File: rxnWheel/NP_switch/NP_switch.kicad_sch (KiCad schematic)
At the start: 11 parts, among them Q6 IRF7404, Q7 Si4162DY

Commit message: Commit
CoMmMMmMMMmits
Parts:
- added Q?: IRF7404, Package_SO:SOIC-8_3.9x4.9mm_P1.27mm, symbol Transistor_FET:IRF7404
- added Q?: Si4162DY, Package_SO:SOIC-8_3.9x4.9mm_P1.27mm, symbol Transistor_FET:Si4162DY
- added R?: 100, Resistor_SMD:R_0805_2012Metric, symbol Device:R
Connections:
- net OUT_PHASE: now also Q?.5 (D), Q?.5 (D), Q?.6 (D), Q?.6 (D), Q?.7 (D), Q?.7 (D), Q?.8 (D), Q?.8 (D); no longer Q6.1 (S), Q6.2 (S), Q6.3 (S), Q7.5 (D), Q7.6 (D), Q7.7 (D), Q7.8 (D), R30.2
- new net: Q?.1 (S), Q?.2 (S), Q?.3 (S), R?.1
- new net: Q6.1 (S), Q6.2 (S), Q6.3 (S), Q7.5 (D), Q7.6 (D), Q7.7 (D), Q7.8 (D), Q?.1 (S), Q?.2 (S), Q?.3 (S), R30.2
- new net DRV_MTR: Q?.4 (G), Q?.4 (G)
- new net GND: R?.2

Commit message: minor changes
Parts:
- renumbered C15 to C11, C16 to C12, D6 to D2, D7 to D3, Q6 to Q2, Q7 to Q3, R26 to R16, R27 to R17, R28 to R18, R29 to R19, R30 to R20
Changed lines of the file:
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@@
     (effects (font (size 1.27 1.27)) (justify right))
   )
-  (symbol (lib_id "Transistor_FET:IRF7404") (at 151.13 101.6 0)
+  (symbol (lib_id "Transistor_FET:IRF7404") (at 151.13 101.6 0) (unit 1)
     (in_bom yes) (on_board yes) (fields_autoplaced)
     (property "Reference" "Q?" (id 0) (at 157.48 100.3299 0)
@@
     (pin "8")
   )
-  (symbol (lib_id "Device:R") (at 82.55 81.28 0)
-    (in_bom yes) (on_board yes) (fields_autoplaced)
-    (property "Reference" "R29" (id 0) (at 85.09 80.0099 0)
+  (symbol (lib_id "Device:R") (at 82.55 81.28 0) (unit 1)
+    (in_bom yes) (on_board yes) (fields_autoplaced)
+    (property "Reference" "R19" (id 0) (at 85.09 80.0099 0)
       (effects (font (size 1.27 1.27)) (justify left))
     )
@@
     (pin "2")
   )
-  (symbol (lib_id "Device:R") (at 60.96 85.09 90)
-    (in_bom yes) (on_board yes) (fields_autoplaced)
-    (property "Reference" "R27" (id 0) (at 60.96 78.74 90))
+  (symbol (lib_id "Device:R") (at 60.96 85.09 90) (unit 1)
+    (in_bom yes) (on_board yes) (fields_autoplaced)
+    (property "Reference" "R17" (id 0) (at 60.96 78.74 90))
     (property "Value" "100" (id 1) (at 60.96 81.28 90))
     (property "Footprint" "Resistor_SMD:R_0805_2012Metric" (id 2) (at 60.96 86.868 90)
@@
     (pin "2")
   )
-  (symbol (lib_id "Diode:BZV55B12") (at 91.44 106.68 270)
-    (in_bom yes) (on_board yes) (fields_autoplaced)
-    (property "Reference" "D6" (id 0) (at 93.98 105.4099 90)
+  (symbol (lib_id "Diode:BZV55B12") (at 91.44 106.68 270) (unit 1)
+    (in_bom yes) (on_board yes) (fields_autoplaced)
+    (property "Reference" "D2" (id 0) (at 93.98 105.4099 90)
       (effects (font (size 1.27 1.27)) (justify left))
     )
@@
     (pin "2")
   )
-  (symbol (lib_id "power:GND") (at 153.67 116.84 0)
+  (symbol (lib_id "power:GND") (at 153.67 116.84 0) (unit 1)
     (in_bom yes) (on_board yes) (fields_autoplaced)
     (property "Reference" "#PWR?" (id 0) (at 153.67 123.19 0)
@@
     (pin "1")
   )
-  (symbol (lib_id "Device:C") (at 67.31 106.68 0)
-    (in_bom yes) (on_board yes) (fields_autoplaced)
-    (property "Reference" "C15" (id 0) (at 71.12 105.4099 0)
+  (symbol (lib_id "Device:C") (at 67.31 106.68 0) (unit 1)
+    (in_bom yes) (on_board yes) (fields_autoplaced)
+    (property "Reference" "C11" (id 0) (at 71.12 105.4099 0)
       (effects (font (size 1.27 1.27)) (justify left))
     )
@@
     (pin "2")
   )
-  (symbol (lib_id "Device:R") (at 59.69 102.87 90)
-    (in_bom yes) (on_board yes) (fields_autoplaced)
-    (property "Reference" "R26" (id 0) (at 59.69 96.52 90))
+  (symbol (lib_id "Device:R") (at 59.69 102.87 90) (unit 1)
+    (in_bom yes) (on_board yes) (fields_autoplaced)
+    (property "Reference" "R16" (id 0) (at 59.69 96.52 90))
     (property "Value" "100" (id 1) (at 59.69 99.06 90))
     (property "Footprint" "Resistor_SMD:R_0805_2012Metric" (id 2) (at 59.69 104.648 90)
@@
     (pin "2")
   )
-  (symbol (lib_id "Device:R") (at 153.67 111.76 0)
+  (symbol (lib_id "Device:R") (at 153.67 111.76 0) (unit 1)
     (in_bom yes) (on_board yes) (fields_autoplaced)
     (property "Reference" "R?" (id 0) (at 156.21 110.4899 0)
@@
     (pin "2")
   )
-  (symbol (lib_id "Diode:BZV55B12") (at 93.98 81.28 270)
-    (in_bom yes) (on_board yes) (fields_autoplaced)
-    (property "Reference" "D7" (id 0) (at 96.52 80.0099 90)
+  (symbol (lib_id "Diode:BZV55B12") (at 93.98 81.28 270) (unit 1)
+    (in_bom yes) (on_board yes) (fields_autoplaced)
+    (property "Reference" "D3" (id 0) (at 96.52 80.0099 90)
       (effects (font (size 1.27 1.27)) (justify left))
     )
@@
     (pin "2")
   )
-  (symbol (lib_id "Device:C") (at 69.85 81.28 0)
-    (in_bom yes) (on_board yes) (fields_autoplaced)
-    (property "Reference" "C16" (id 0) (at 73.66 80.0099 0)
+  (symbol (lib_id "Device:C") (at 69.85 81.28 0) (unit 1)
+    (in_bom yes) (on_board yes) (fields_autoplaced)
+    (property "Reference" "C12" (id 0) (at 73.66 80.0099 0)
       (effects (font (size 1.27 1.27)) (justify left))
     )
@@
     (pin "2")
   )
-  (symbol (lib_id "Device:R") (at 80.01 106.68 0)
-    (in_bom yes) (on_board yes) (fields_autoplaced)
-    (property "Reference" "R28" (id 0) (at 82.55 105.4099 0)
+  (symbol (lib_id "Device:R") (at 80.01 106.68 0) (unit 1)
+    (in_bom yes) (on_board yes) (fields_autoplaced)
+    (property "Reference" "R18" (id 0) (at 82.55 105.4099 0)
       (effects (font (size 1.27 1.27)) (justify left))
     )
@@
     (pin "2")
   )
-  (symbol (lib_id "Transistor_FET:Si4162DY") (at 107.95 102.87 0)
-    (in_bom yes) (on_board yes) (fields_autoplaced)
-    (property "Reference" "Q7" (id 0) (at 114.3 101.5999 0)
+  (symbol (lib_id "Transistor_FET:Si4162DY") (at 107.95 102.87 0) (unit 1)
+    (in_bom yes) (on_board yes) (fields_autoplaced)
+    (property "Reference" "Q3" (id 0) (at 114.3 101.5999 0)
       (effects (font (size 1.27 1.27)) (justify left))
     )
@@
     (pin "8")
   )
-  (symbol (lib_id "Device:R") (at 124.46 90.17 0)
-    (in_bom yes) (on_board yes) (fields_autoplaced)
-    (property "Reference" "R30" (id 0) (at 127 88.8999 0)
+  (symbol (lib_id "Device:R") (at 124.46 90.17 0) (unit 1)
+    (in_bom yes) (on_board yes) (fields_autoplaced)
+    (property "Reference" "R20" (id 0) (at 127 88.8999 0)
       (effects (font (size 1.27 1.27)) (justify left))
     )
@@
     (pin "2")
   )
-  (symbol (lib_id "Transistor_FET:IRF7404") (at 107.95 85.09 0)
-    (in_bom yes) (on_board yes) (fields_autoplaced)
-    (property "Reference" "Q6" (id 0) (at 114.3 83.8199 0)
+  (symbol (lib_id "Transistor_FET:IRF7404") (at 107.95 85.09 0) (unit 1)
+    (in_bom yes) (on_board yes) (fields_autoplaced)
+    (property "Reference" "Q2" (id 0) (at 114.3 83.8199 0)
       (effects (font (size 1.27 1.27)) (justify left))
     )
@@
     (pin "8")
   )
-  (symbol (lib_id "Transistor_FET:Si4162DY") (at 138.43 91.44 270)
+  (symbol (lib_id "Transistor_FET:Si4162DY") (at 138.43 91.44 270) (unit 1)
     (in_bom yes) (on_board yes) (fields_autoplaced)
     (property "Reference" "Q?" (id 0) (at 138.43 99.06 90))

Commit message: Brake
commmit
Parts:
- removed Q?: Si4162DY, Package_SO:SOIC-8_3.9x4.9mm_P1.27mm, symbol Transistor_FET:Si4162DY
- removed R?: 100, Resistor_SMD:R_0805_2012Metric, symbol Device:R
- added Q?: Si4162DY, Package_SO:SOIC-8_3.9x4.9mm_P1.27mm, symbol Transistor_FET:Si4162DY
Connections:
- net DRV_MTR: now also Q?.4 (G)
- net OUT_PHASE: now also Q?.1 (S), Q?.2 (S), Q?.3 (S), Q?.1 (S), Q?.2 (S), Q?.3 (S); no longer Q?.5 (D), Q?.6 (D), Q?.7 (D), Q?.8 (D)
- net at Q2.1 (S), Q2.2 (S), Q2.3 (S)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: now also Q?.5 (D), Q?.6 (D), Q?.7 (D), Q?.8 (D)
- new net BRK_OUT: Q?.5 (D), Q?.6 (D), Q?.7 (D), Q?.8 (D)
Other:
- moved on the sheet: Q?

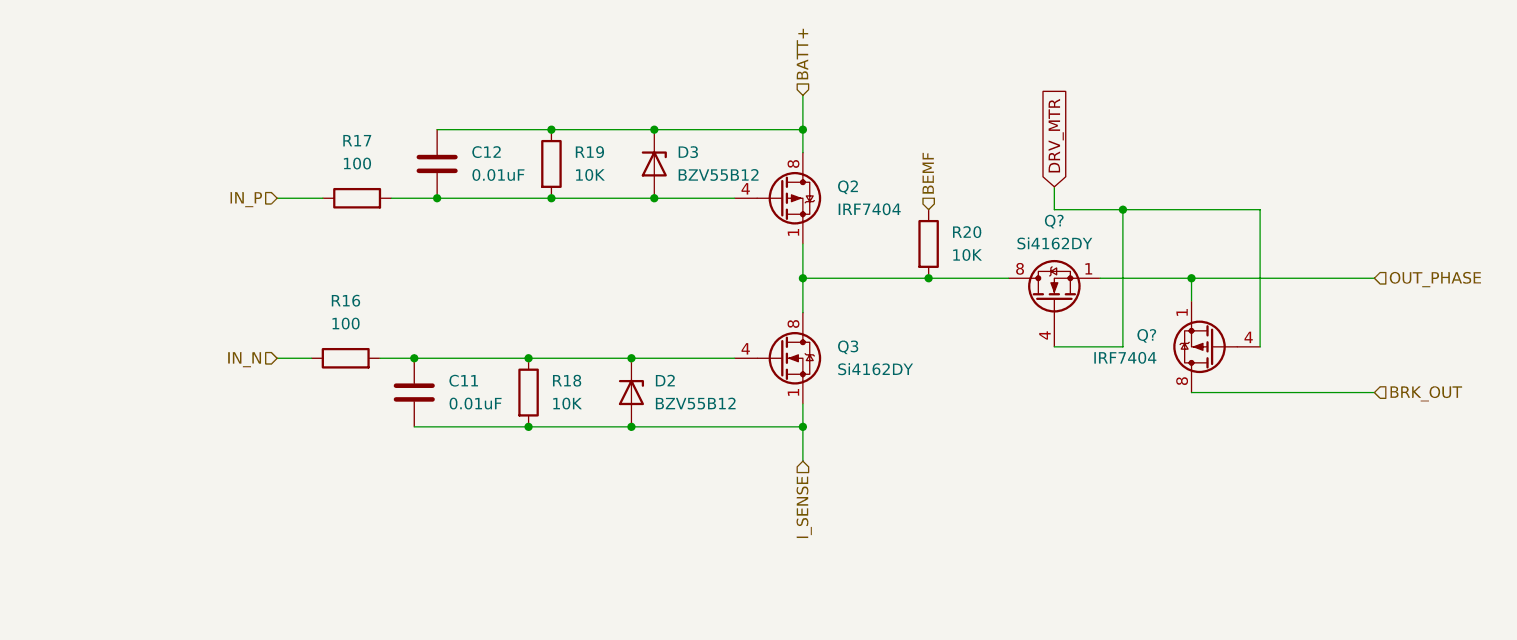
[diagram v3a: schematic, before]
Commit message: LED
led
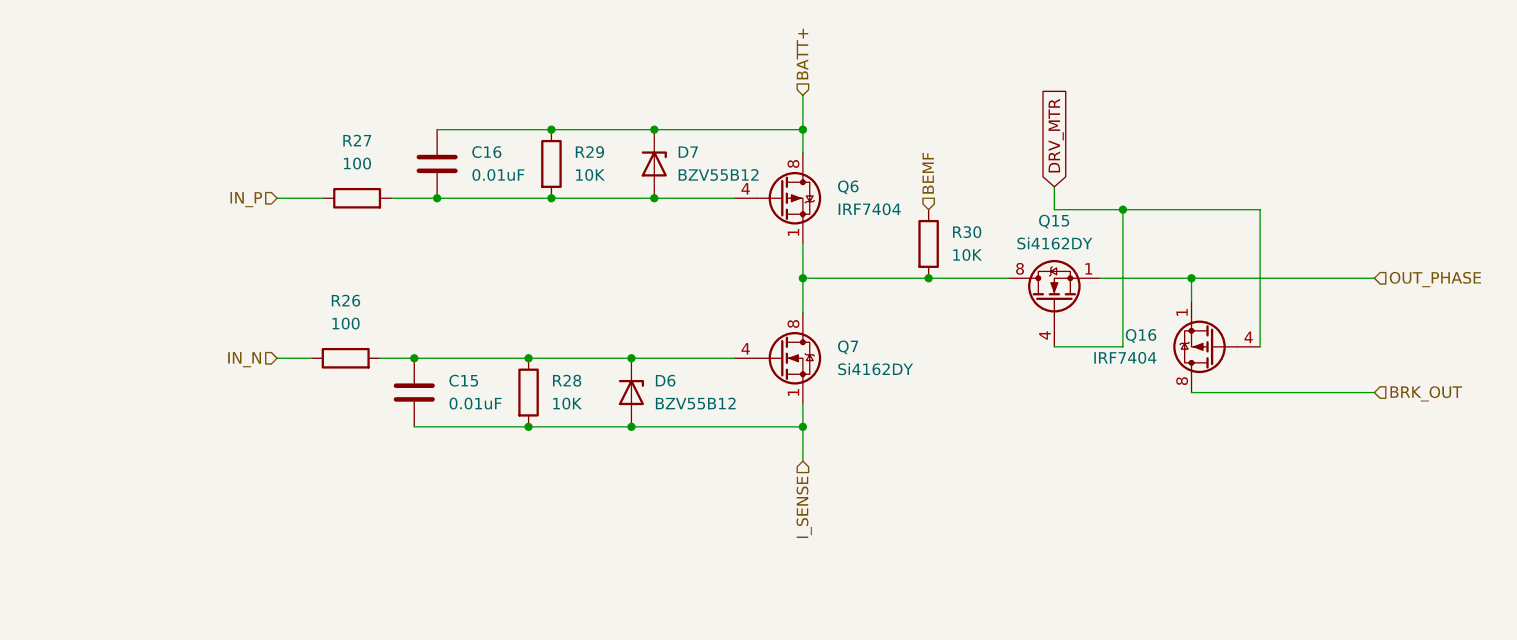
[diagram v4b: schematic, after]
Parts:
- gave numbers to parts that had none: 2
- renumbered C11 to C15, C12 to C16, D2 to D6, D3 to D7, Q2 to Q6, Q3 to Q7, R16 to R26, R17 to R27, R18 to R28, R19 to R29, R20 to R30
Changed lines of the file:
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@@
   (symbol (lib_id "Transistor_FET:IRF7404") (at 156.21 101.6 180)
     (in_bom yes) (on_board yes) (fields_autoplaced)
-    (property "Reference" "Q?" (id 0) (at 149.86 100.3299 0)
+    (property "Reference" "Q16" (id 0) (at 149.86 100.3299 0)
       (effects (font (size 1.27 1.27)) (justify left))
     )
@@
   (symbol (lib_id "Device:R") (at 82.55 81.28 0)
     (in_bom yes) (on_board yes) (fields_autoplaced)
-    (property "Reference" "R19" (id 0) (at 85.09 80.0099 0)
+    (property "Reference" "R29" (id 0) (at 85.09 80.0099 0)
       (effects (font (size 1.27 1.27)) (justify left))
     )
@@
   (symbol (lib_id "Device:R") (at 60.96 85.09 90)
     (in_bom yes) (on_board yes) (fields_autoplaced)
-    (property "Reference" "R17" (id 0) (at 60.96 78.74 90))
+    (property "Reference" "R27" (id 0) (at 60.96 78.74 90))
     (property "Value" "100" (id 1) (at 60.96 81.28 90))
     (property "Footprint" "Resistor_SMD:R_0805_2012Metric" (id 2) (at 60.96 86.868 90)
@@
   (symbol (lib_id "Diode:BZV55B12") (at 91.44 106.68 270)
     (in_bom yes) (on_board yes) (fields_autoplaced)
-    (property "Reference" "D2" (id 0) (at 93.98 105.4099 90)
+    (property "Reference" "D6" (id 0) (at 93.98 105.4099 90)
       (effects (font (size 1.27 1.27)) (justify left))
     )
@@
   (symbol (lib_id "Transistor_FET:Si4162DY") (at 138.43 96.52 90)
     (in_bom yes) (on_board yes)
-    (property "Reference" "Q?" (id 0) (at 138.43 87.63 90))
+    (property "Reference" "Q15" (id 0) (at 138.43 87.63 90))
     (property "Value" "Si4162DY" (id 1) (at 138.43 90.17 90))
     (property "Footprint" "Package_SO:SOIC-8_3.9x4.9mm_P1.27mm" (id 2) (at 140.97 91.44 0)
@@
   (symbol (lib_id "Device:C") (at 67.31 106.68 0)
     (in_bom yes) (on_board yes) (fields_autoplaced)
-    (property "Reference" "C11" (id 0) (at 71.12 105.4099 0)
+    (property "Reference" "C15" (id 0) (at 71.12 105.4099 0)
       (effects (font (size 1.27 1.27)) (justify left))
     )
@@
   (symbol (lib_id "Device:R") (at 59.69 102.87 90)
     (in_bom yes) (on_board yes) (fields_autoplaced)
-    (property "Reference" "R16" (id 0) (at 59.69 96.52 90))
+    (property "Reference" "R26" (id 0) (at 59.69 96.52 90))
     (property "Value" "100" (id 1) (at 59.69 99.06 90))
     (property "Footprint" "Resistor_SMD:R_0805_2012Metric" (id 2) (at 59.69 104.648 90)
@@
   (symbol (lib_id "Diode:BZV55B12") (at 93.98 81.28 270)
     (in_bom yes) (on_board yes) (fields_autoplaced)
-    (property "Reference" "D3" (id 0) (at 96.52 80.0099 90)
+    (property "Reference" "D7" (id 0) (at 96.52 80.0099 90)
       (effects (font (size 1.27 1.27)) (justify left))
     )
@@
   (symbol (lib_id "Device:C") (at 69.85 81.28 0)
     (in_bom yes) (on_board yes) (fields_autoplaced)
-    (property "Reference" "C12" (id 0) (at 73.66 80.0099 0)
+    (property "Reference" "C16" (id 0) (at 73.66 80.0099 0)
       (effects (font (size 1.27 1.27)) (justify left))
     )
@@
   (symbol (lib_id "Device:R") (at 80.01 106.68 0)
     (in_bom yes) (on_board yes) (fields_autoplaced)
-    (property "Reference" "R18" (id 0) (at 82.55 105.4099 0)
+    (property "Reference" "R28" (id 0) (at 82.55 105.4099 0)
       (effects (font (size 1.27 1.27)) (justify left))
     )
@@
   (symbol (lib_id "Transistor_FET:Si4162DY") (at 107.95 102.87 0)
     (in_bom yes) (on_board yes) (fields_autoplaced)
-    (property "Reference" "Q3" (id 0) (at 114.3 101.5999 0)
+    (property "Reference" "Q7" (id 0) (at 114.3 101.5999 0)
       (effects (font (size 1.27 1.27)) (justify left))
     )
@@
   (symbol (lib_id "Device:R") (at 124.46 90.17 0)
     (in_bom yes) (on_board yes) (fields_autoplaced)
-    (property "Reference" "R20" (id 0) (at 127 88.8999 0)
+    (property "Reference" "R30" (id 0) (at 127 88.8999 0)
       (effects (font (size 1.27 1.27)) (justify left))
     )
@@
   (symbol (lib_id "Transistor_FET:IRF7404") (at 107.95 85.09 0)
     (in_bom yes) (on_board yes) (fields_autoplaced)
-    (property "Reference" "Q2" (id 0) (at 114.3 83.8199 0)
-      (effects (font (size 1.27 1.27)) (justify left))
-    )
+    (property "Reference" "Q6" (id 0) (at 114.3 83.8199 0)
+      (effects (font (size 1.27 1.27)) (justify left))
+    )

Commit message: cleanup and corrections
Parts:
- removed R26, R27: 100, Resistor_SMD:R_0805_2012Metric, symbol Device:R
- added Q17: ~, symbol Transistor_BJT:2N3904
- added Q18: 2N3904, Package_TO_SOT_THT:TO-92_Inline, symbol Transistor_BJT:2N3904
- added R1, R2: 100, Resistor_SMD:R_0805_2012Metric, symbol Device:R
- added R11, R12, R4, R5: 10K, Resistor_SMD:R_0805_2012Metric, symbol Device:R
- Q2: renamed from Q6; value IRF7404 -> (none); footprint Package_SO:SOIC-8_3.9x4.9mm_P1.27mm -> (none)
- renumbered C15 to C11, C16 to C12, D6 to D2, D7 to D3, Q15 to Q11, Q16 to Q12, Q7 to Q3, R28 to R18, R29 to R19, R30 to R20
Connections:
- net BATT+: now also Q2.1 (S), Q2.2 (S), Q2.3 (S); no longer Q2.5 (D), Q2.6 (D), Q2.7 (D), Q2.8 (D)
- net IN_N: now also R2.1
- net IN_P: now also R1.1
- net at C12.2, D3.2 (A), Q2.4 (G)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: now also Q17.1 (E), R11.1
- net at C11.1, D2.1 (K), Q3.4 (G)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: now also Q18.1 (E), R12.1
- net at Q11.5 (D), Q11.6 (D), Q11.7 (D)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: now also Q2.5 (D), Q2.6 (D), Q2.7 (D), Q2.8 (D); no longer Q2.1 (S), Q2.2 (S), Q2.3 (S)
- net I_SENSE renamed GND
- net GND: now also R11.2, R12.2, R4.2, R5.2
- new net: Q17.2 (B), R1.2, R4.1
- new net: Q18.2 (B), R2.2, R5.1
- new net +5V: Q17.3 (C), Q18.3 (C)

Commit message: changes
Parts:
- removed C11, C12: 0.01uF, Capacitor_SMD:C_0805_2012Metric, symbol Device:C
- removed D2, D3: BZV55B12, Diode_SMD:D_MiniMELF, symbol Diode:BZV55B12
- removed Q11: Si4162DY, Package_SO:SOIC-8_3.9x4.9mm_P1.27mm, symbol Transistor_FET:Si4162DY
- removed Q17: ~, symbol Transistor_BJT:2N3904
- removed Q18: 2N3904, Package_TO_SOT_THT:TO-92_Inline, symbol Transistor_BJT:2N3904
- removed Q2: (no value), symbol Transistor_FET:IRF7404
- removed R1, R2: 100, Resistor_SMD:R_0805_2012Metric, symbol Device:R
- removed R11, R12, R18, R19, R20, R4, R5: 10K, Resistor_SMD:R_0805_2012Metric, symbol Device:R
- added C? (x4): (no value), Capacitor_SMD:C_0805_2012Metric, symbol Device:C
- added Q? (x2): (no value), symbol Transistor_FET:IRF7404
- added U? (x2): (no value), symbol Driver_FET:MCP14A0902xMNY
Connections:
- net BATT+: now also Q?.1 (S), Q?.2 (S), Q?.3 (S)
- net DRV_MTR: now also Q?.4 (G)
- net GND: now also C?.2, C?.2, C?.2, C?.2, U?.4 (GND), U?.4 (GND), U?.5 (GND), U?.5 (GND), U?.9 (GND), U?.9 (GND)
- net OUT_PHASE: now also Q?.5 (D), Q?.6 (D), Q?.7 (D), Q?.8 (D)
- net at Q3.4 (G): now also U?.6 (OUT), U?.7 (OUT)
- net at Q3.5 (D), Q3.6 (D), Q3.7 (D)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: now also Q?.1 (S), Q?.2 (S), Q?.3 (S), Q?.5 (D), Q?.6 (D), Q?.7 (D), Q?.8 (D)
- new net: Q?.4 (G), U?.6 (OUT), U?.7 (OUT)
- new net IN_H: U?.2 (IN)
- new net IN_L: U?.2 (IN)
- new net VBUS: C?.1, C?.1, C?.1, C?.1, U?.1 (VDD), U?.1 (VDD), U?.3 (EN), U?.3 (EN), U?.8 (VDD), U?.8 (VDD)

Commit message: minor changes
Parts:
- removed Q12: IRF7404, Package_SO:SOIC-8_3.9x4.9mm_P1.27mm, symbol Transistor_FET:IRF7404
- removed Q?: (no value), symbol Transistor_FET:IRF7404
- added C?: (no value), symbol Device:C
- added C?: (no value), Capacitor_SMD:C_0805_2012Metric, symbol Device:C
- C? (x2): value (none) -> 0.1uF
- C? (x2): value (none) -> 1uF
- Q?: value (none) -> IRF7404; footprint (none) -> Package_SO:SOIC-8_3.9x4.9mm_P1.27mm
- U?: value (none) -> MCP14A0902xMNY
- U?: value (none) -> MCP14A0902xMNY; footprint (none) -> Package_DFN_QFN:TDFN-8-1EP_3x2mm_P0.5mm_EP1.3x1.4mm
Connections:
- net GND: now also C?.2, C?.2
- net OUT_PHASE: now also Q3.5 (D), Q3.6 (D), Q3.7 (D), Q3.8 (D), Q?.5 (D), Q?.6 (D), Q?.7 (D), Q?.8 (D)
- net at Q3.4 (G), U?.6 (OUT), U?.7 (OUT): now also C?.1
- net at Q?.4 (G), U?.6 (OUT), U?.7 (OUT): now also C?.1
